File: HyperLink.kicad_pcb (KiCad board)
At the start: 2 copper layers, 35 x 24 mm, 45 parts, among them J1 USB_C_Receptacle_USB2.0, J2 Conn_02x05_Odd_Even, J3 Conn_02x05_Odd_Even, SW1 SW_Push, U1 ESP32-C3, U2 PESD2USB5UXT, U3 MIC5504-3.3YM5, Y1 ABM11W-40.0000MHZ-8-B1U-T3

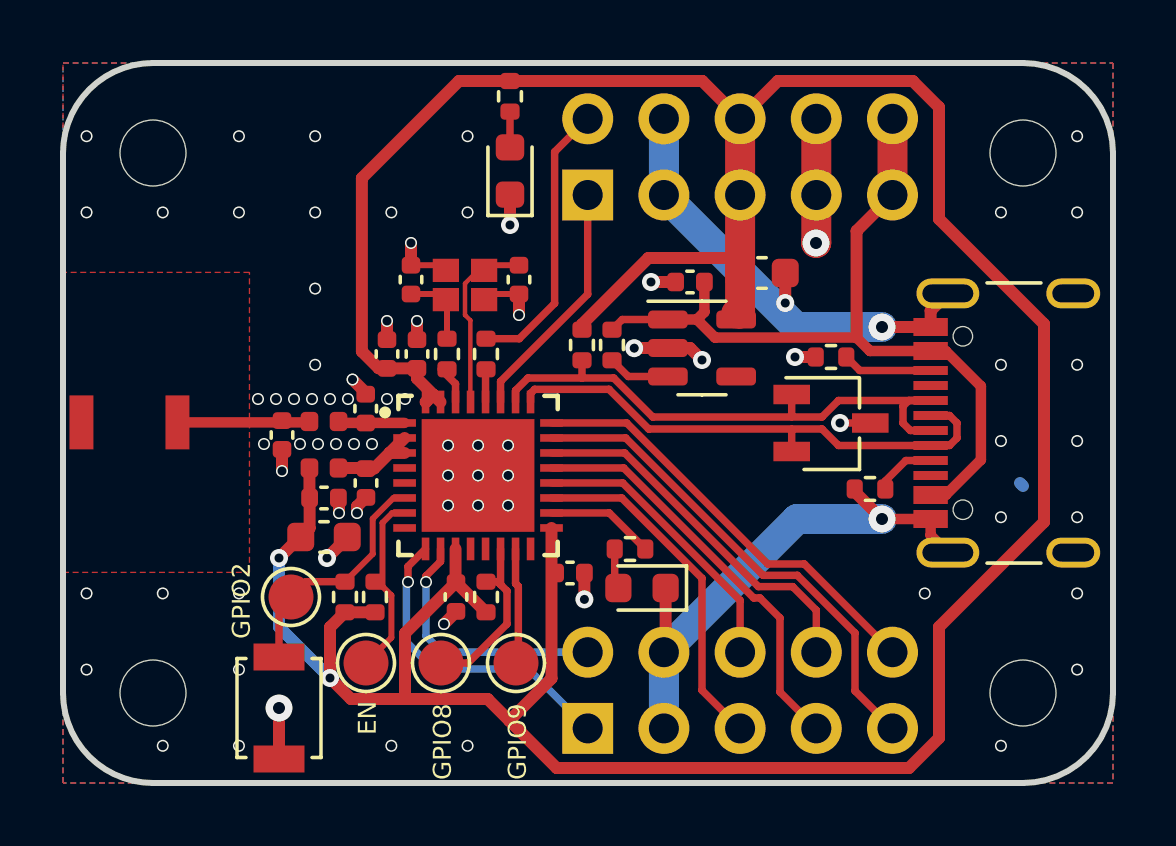
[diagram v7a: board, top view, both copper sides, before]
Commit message: Change connector thermal reliefs, various vias
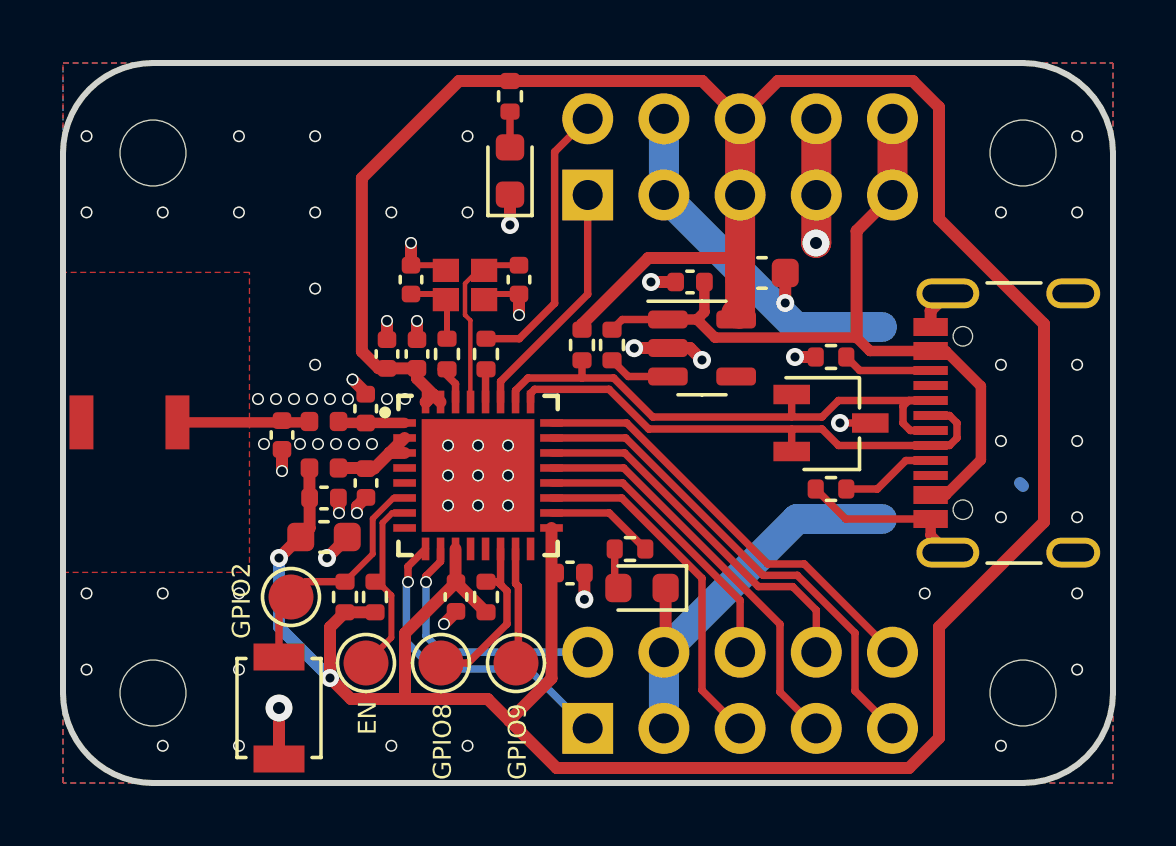
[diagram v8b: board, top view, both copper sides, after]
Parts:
- moved R8 1.30 mm to (144.6, 84.2)
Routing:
- net /CC1: track 2.06 -> 3.20 mm
- net GND: track 55.8 -> 55.5 mm, vias 79 -> 77
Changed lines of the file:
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@@
   )
   (footprint "Resistor_SMD:R_0402_1005Metric" (layer "F.Cu")
-    (at 145.9 84.2 180)
+    (at 144.6 84.2 180)
     (descr "Resistor SMD 0402 (1005 Metric), square (rectangular) end terminal, IPC_7351 nominal, (Body size source: IPC-SM-782 page 72, https://www.pcb-3d.com/wordpress/wp-content/uploads/ipc-sm-782a_amendment_1_and_2.pdf), generated with kicad-footprint-generator")
     (tags "resistor")
@@
       (net 5 "GND") (pinfunction "GND") (pintype "passive"))
     (pad "S1" thru_hole oval locked (at -4.32 -3.105 90) (size 1 2.1) (drill oval 0.6 1.7) (layers "*.Cu" "*.Mask" "F.Paste")
-      (net 5 "GND") (pinfunction "SHIELD") (pintype "passive") (zone_connect 2))
+      (net 5 "GND") (pinfunction "SHIELD") (pintype "passive"))
     (pad "S1" thru_hole oval locked (at -4.32 1.075 90) (size 1 1.8) (drill oval 0.6 1.4) (layers "*.Cu" "*.Mask" "F.Paste")
-      (net 5 "GND") (pinfunction "SHIELD") (pintype "passive") (zone_connect 2))
+      (net 5 "GND") (pinfunction "SHIELD") (pintype "passive"))
     (pad "S1" thru_hole oval locked (at 4.32 -3.105 90) (size 1 2.1) (drill oval 0.6 1.7) (layers "*.Cu" "*.Mask" "F.Paste")
-      (net 5 "GND") (pinfunction "SHIELD") (pintype "passive") (zone_connect 2))
+      (net 5 "GND") (pinfunction "SHIELD") (pintype "passive"))
     (pad "S1" thru_hole oval locked (at 4.32 1.075 90) (size 1 1.8) (drill oval 0.6 1.4) (layers "*.Cu" "*.Mask" "F.Paste")
-      (net 5 "GND") (pinfunction "SHIELD") (pintype "passive") (zone_connect 2))
+      (net 5 "GND") (pinfunction "SHIELD") (pintype "passive"))
     (model "${KICAD7_3DMODEL_DIR}/Connector_USB.3dshapes/USB_C_Receptacle_GCT_USB4105-xx-A_16P_TopMnt_Horizontal.wrl"
       (offset (xyz 0 0 0))
@@
   (segment (start 128.65 80.55) (end 129.09 80.99) (width 0.4) (layer "F.Cu") (net 5))
   (segment (start 133.9 74.3875) (end 133.9 75.4) (width 0.4) (layer "F.Cu") (net 5))
+  (segment (start 144.09 84.2) (end 145.09 85.2) (width 0.25) (layer "F.Cu") (net 5))
   (segment (start 139.42 77.3) (end 138.6 77.3) (width 0.4) (layer "F.Cu") (net 5))
   (segment (start 130.8 79.22) (end 130.8 78.6) (width 0.4) (layer "F.Cu") (net 5))
@@
   (segment (start 144.11 74.4) (end 144.11 71.86) (width 1) (layer "F.Cu") (net 5))
   (segment (start 131.590001 76.74) (end 131.763001 76.913) (width 0.2) (layer "F.Cu") (net 5))
-  (segment (start 146.3 85.2) (end 147.92 85.2) (width 0.35) (layer "F.Cu") (net 5))
   (segment (start 130.6 76.74) (end 131.590001 76.74) (width 0.2) (layer "F.Cu") (net 5))
   (segment (start 143.075 78) (end 143.075 77) (width 0.4) (layer "F.Cu") (net 5))
-  (segment (start 145.39 84.29) (end 146.3 85.2) (width 0.4) (layer "F.Cu") (net 5))
   (segment (start 129.8 79.22) (end 129.8 78.6) (width 0.4) (layer "F.Cu") (net 5))
   (segment (start 126.2 93.2) (end 126.2 91.5) (width 0.4) (layer "F.Cu") (net 5))
@@
   (segment (start 139.0875 87.5) (end 139.0875 89.5825) (width 0.4) (layer "F.Cu") (net 5))
   (segment (start 138.046557 79.5) (end 139.1625 79.5) (width 0.4) (layer "F.Cu") (net 5))
-  (segment (start 146.3 78.8) (end 147.92 78.8) (width 0.4) (layer "F.Cu") (net 5))
-  (segment (start 145.39 84.2) (end 145.39 84.29) (width 0.4) (layer "F.Cu") (net 5))
   (segment (start 133.224001 77.7) (end 133.037001 77.887) (width 0.2) (layer "F.Cu") (net 5))
   (segment (start 139.0875 89.5825) (end 139.03 89.64) (width 0.4) (layer "F.Cu") (net 5))
   (segment (start 139.9 79.5) (end 139.1625 79.5) (width 0.4) (layer "F.Cu") (net 5))
+  (segment (start 145.09 85.2) (end 147.92 85.2) (width 0.25) (layer "F.Cu") (net 5))
   (segment (start 128.475 85.825) (end 128.475 85.8) (width 0.4) (layer "F.Cu") (net 5))
   (segment (start 134.2 78.4) (end 134.2 77.7) (width 0.4) (layer "F.Cu") (net 5))
@@
   (via (at 124.865 92.759999) (size 0.4) (drill 0.3) (layers "F.Cu" "B.Cu") (free) (net 5))
   (via (at 132.485 74.979999) (size 0.4) (drill 0.3) (layers "F.Cu" "B.Cu") (free) (net 5))
-  (via (at 146.3 78.8) (size 0.9) (drill 0.4) (layers "F.Cu" "B.Cu") (free) (net 5))
   (via (at 133.834851 84.7487) (size 0.4) (drill 0.3) (layers "F.Cu" "B.Cu") (net 5))
   (via (at 126.7 81.2) (size 0.4) (drill 0.3) (layers "F.Cu" "B.Cu") (free) (net 5))
@@
   (via (at 129.945 92.759999) (size 0.4) (drill 0.3) (layers "F.Cu" "B.Cu") (free) (net 5))
   (via (at 130.8 78.6) (size 0.4) (drill 0.3) (layers "F.Cu" "B.Cu") (free) (net 5))
-  (via (at 146.3 85.2) (size 0.9) (drill 0.4) (layers "F.Cu" "B.Cu") (free) (net 5))
   (via (at 125.7 82.7) (size 0.4) (drill 0.3) (layers "F.Cu" "B.Cu") (free) (net 5))
   (via (at 150.265 85.139999) (size 0.4) (drill 0.3) (layers "F.Cu" "B.Cu") (free) (net 5))
@@
   (segment (start 135.283551 83.9987) (end 137.656594 83.9987) (width 0.25) (layer "F.Cu") (net 27))
   (segment (start 137.656594 83.9987) (end 141.57 87.912106) (width 0.25) (layer "F.Cu") (net 27))
-  (segment (start 142.022052 87.831) (end 142.231 87.831) (width 0.25) (layer "F.Cu") (net 28))
-  (segment (start 142.231 87.831) (end 142.9 88.5) (width 0.25) (layer "F.Cu") (net 28))
   (segment (start 142.9 90.97) (end 144.11 92.18) (width 0.25) (layer "F.Cu") (net 28))
+  (segment (start 142.9 88.708948) (end 142.9 90.97) (width 0.25) (layer "F.Cu") (net 28))
   (segment (start 135.283551 83.4987) (end 137.689752 83.4987) (width 0.25) (layer "F.Cu") (net 28))
-  (segment (start 142.9 88.5) (end 142.9 90.97) (width 0.25) (layer "F.Cu") (net 28))
-  (segment (start 137.689752 83.4987) (end 142.022052 87.831) (width 0.25) (layer "F.Cu") (net 28))
+  (segment (start 137.689752 83.4987) (end 142.9 88.708948) (width 0.25) (layer "F.Cu") (net 28))
   (segment (start 144.11 88.243158) (end 144.11 89.64) (width 0.25) (layer "F.Cu") (net 29))
   (segment (start 137.722909 82.998699) (end 142.17821 87.454) (width 0.25) (layer "F.Cu") (net 29))
@@
   (segment (start 131.099503 89.099503) (end 131.64 89.64) (width 0.25) (layer "B.Cu") (net 33))
   (segment (start 133.084851 81.3) (end 133.084851 80.365149) (width 0.25) (layer "F.Cu") (net 34))
-  (segment (start 147.095 83.25) (end 146.41 83.935) (width 0.25) (layer "F.Cu") (net 35))
   (segment (start 147.92 83.25) (end 147.095 83.25) (width 0.25) (layer "F.Cu") (net 35))
-  (segment (start 146.41 83.935) (end 146.41 84.2) (width 0.25) (layer "F.Cu") (net 35))
+  (segment (start 146.145 84.2) (end 145.11 84.2) (width 0.25) (layer "F.Cu") (net 35))
+  (segment (start 147.095 83.25) (end 146.145 84.2) (width 0.25) (layer "F.Cu") (net 35))
   (segment (start 145.56 80.25) (end 147.92 80.25) (width 0.25) (layer "F.Cu") (net 36))
   (segment (start 145.11 79.8) (end 145.56 80.25) (width 0.25) (layer "F.Cu") (net 36))
